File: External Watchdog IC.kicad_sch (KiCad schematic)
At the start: 5 parts, among them U4 TPS3823A-33DBVR

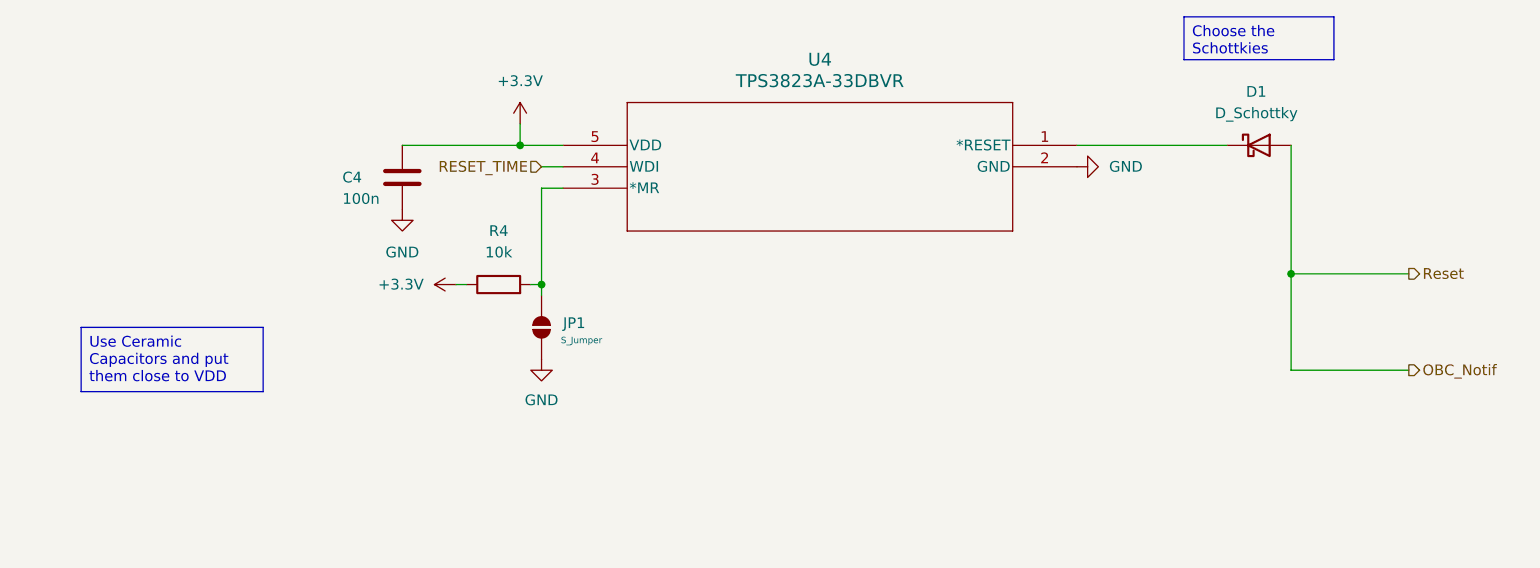
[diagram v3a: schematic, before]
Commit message: added current sensing and e-fuses
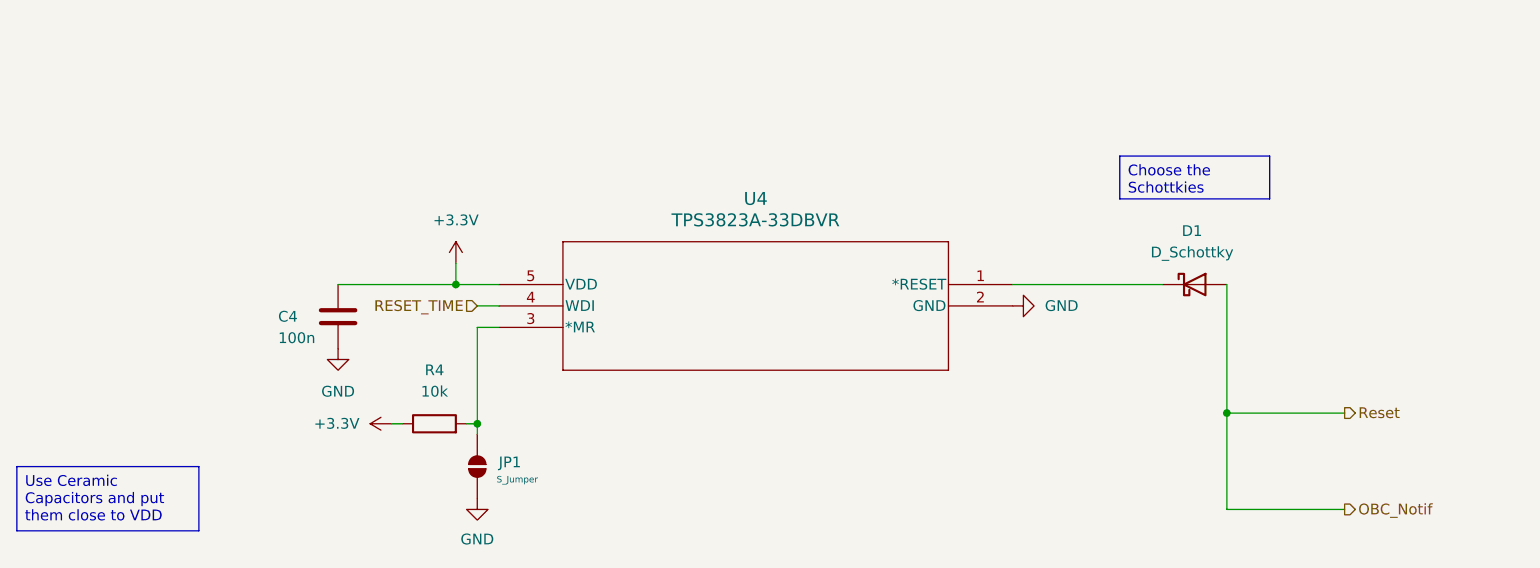
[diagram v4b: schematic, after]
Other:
- moved on the sheet: C4, D1, JP1, R4, U4

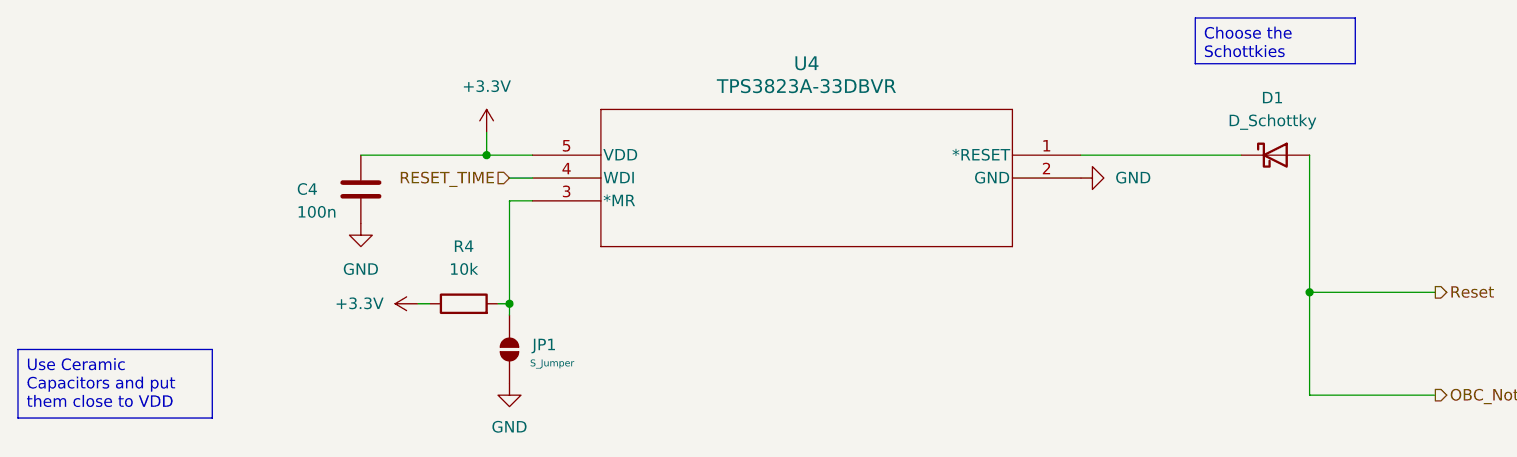
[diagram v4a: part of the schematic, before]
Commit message: Added connectors to schematic
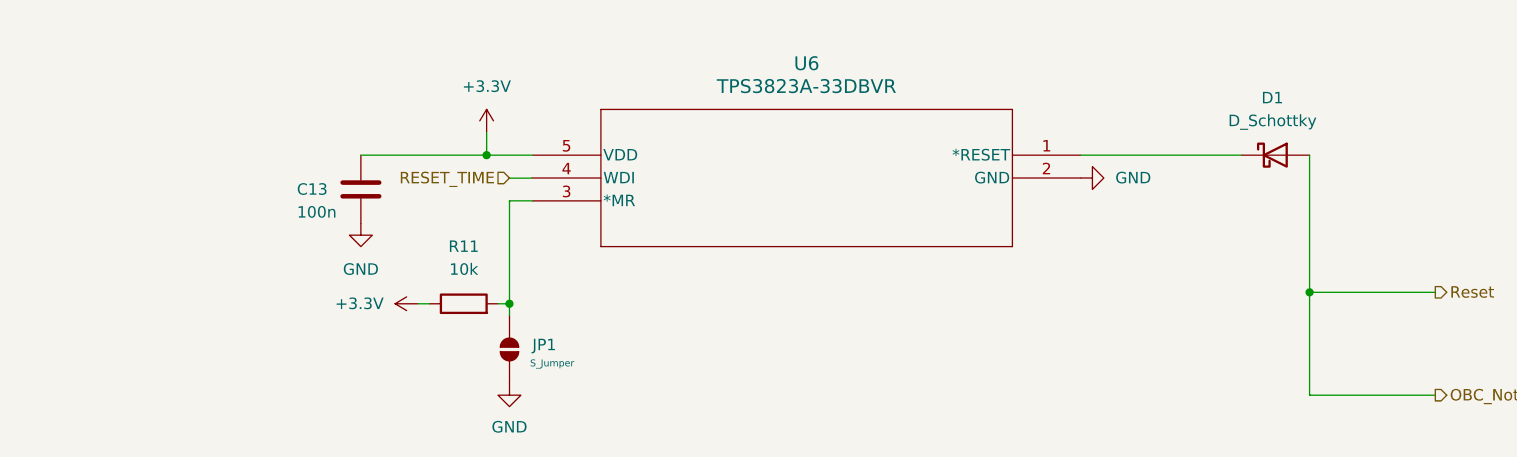
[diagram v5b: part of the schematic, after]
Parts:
- R11: renamed from R4; footprint (none) -> Resistor_SMD:R_0805_2012Metric; MANUFACTURER (none) -> Digikey; MANUFACTURER_PART_NUMBER (none) -> TNPW080510K0FEEA
- U6: renamed from U4; footprint DBV5 -> Package_TO_SOT_SMD:SOT-23-5_HandSoldering
- renumbered C4 to C13
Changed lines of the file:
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@@
 		(company "QSET (Jaron Cyna)")
-	)
-	(text_box "Use Ceramic Capacitors and put them close to VDD"
-		(exclude_from_sim no)
-		(at 55.88 110.49 0)
-		(size 21.59 7.62)
-		(margins 0.9525 0.9525 0.9525 0.9525)
-		(stroke
-			(width 0)
-			(type solid)
-		)
-		(fill
-			(type color)
-			(color 158 218 255 1)
-		)
-		(effects
-			(font
-				(size 1.27 1.27)
-			)
-			(justify left top)
-		)
-	)
-	(text_box "Choose the Schottkies"
-		(exclude_from_sim no)
-		(at 186.69 73.66 0)
-		(size 17.78 5.08)
-		(margins 0.9525 0.9525 0.9525 0.9525)
-		(stroke
-			(width 0)
-			(type solid)
-		)
-		(fill
-			(type color)
-			(color 158 218 255 1)
-		)
-		(effects
-			(font
-				(size 1.27 1.27)
-			)
-			(justify left top)
-		)
 	)
 	(junction
@@
 		(exclude_from_sim no)
 		(in_bom yes)
-		(on_board yes)
+		(on_board no)
 		(dnp no)
 		(fields_autoplaced yes)
@@
 		(dnp no)
 		(fields_autoplaced yes)
-		(property "Reference" "#PWR010"
+		(property "Reference" "#PWR026"
 			(at 93.98 102.87 0)
 			(effects
@@
 			(project ""
 				(path "/8f246f89-1ec7-4136-9977-839b50e116ed/61eb8b07-a516-4600-8bd8-c85438ae98cc"
-					(reference "#PWR010")
+					(reference "#PWR026")
 					(unit 1)
 				)
@@
 		(dnp no)
 		(fields_autoplaced yes)
-		(property "Reference" "R4"
+		(property "Reference" "R11"
 			(at 105.41 99.06 90)
 			(effects
@@
 			)
 		)
-		(property "Footprint" ""
+		(property "Footprint" "Resistor_SMD:R_0805_2012Metric"
 			(at 105.41 107.188 90)
 			(effects
@@
 			)
 		)
+		(property "MANUFACTURER_PART_NUMBER" "TNPW080510K0FEEA"
+			(at 105.41 105.41 0)
+			(effects
+				(font
+					(size 1.27 1.27)
+				)
+				(hide yes)
+			)
+		)
+		(property "MANUFACTURER" "Digikey"
+			(at 105.41 105.41 0)
+			(effects
+				(font
+					(size 1.27 1.27)
+				)
+				(hide yes)
+			)
+		)
 		(pin "1"
 		)
@@
 			(project "EPS_mppt_board"
 				(path "/8f246f89-1ec7-4136-9977-839b50e116ed/61eb8b07-a516-4600-8bd8-c85438ae98cc"
-					(reference "R4")
+					(reference "R11")
 					(unit 1)
 				)
@@
 		(on_board yes)
 		(dnp no)
-		(property "Reference" "C4"
+		(property "Reference" "C13"
 			(at 86.868 92.71 0)
 			(effects
@@
 			(project ""
 				(path "/8f246f89-1ec7-4136-9977-839b50e116ed/61eb8b07-a516-4600-8bd8-c85438ae98cc"
-					(reference "C4")
+					(reference "C13")
 					(unit 1)
 				)
@@
 		(dnp no)
 		(fields_autoplaced yes)
-		(property "Reference" "#PWR08"
+		(property "Reference" "#PWR024"
 			(at 107.95 90.17 0)
 			(effects
@@
 			(project ""
 				(path "/8f246f89-1ec7-4136-9977-839b50e116ed/61eb8b07-a516-4600-8bd8-c85438ae98cc"
-					(reference "#PWR08")
+					(reference "#PWR024")
 					(unit 1)
 				)
@@
 		(dnp no)
 		(fields_autoplaced yes)
-		(property "Reference" "#PWR011"
+		(property "Reference" "#PWR027"
 			(at 104.14 105.41 0)
 			(effects
@@
 			(project "EPS_mppt_board"
 				(path "/8f246f89-1ec7-4136-9977-839b50e116ed/61eb8b07-a516-4600-8bd8-c85438ae98cc"
-					(reference "#PWR011")
+					(reference "#PWR027")
 					(unit 1)
 				)
@@
 		(on_board yes)
 		(dnp no)
-		(property "Reference" "U4"
+		(property "Reference" "U6"
 			(at 143.51 78.74 0)
 			(effects
@@
 			)
 		)
-		(property "Footprint" "DBV5"
+		(property "Footprint" "Package_TO_SOT_SMD:SOT-23-5_HandSoldering"
 			(at 173.99 88.9 0)
 			(effects
@@
 			(project ""
 				(path "/8f246f89-1ec7-4136-9977-839b50e116ed/61eb8b07-a516-4600-8bd8-c85438ae98cc"
-					(reference "U4")
+					(reference "U6")
 					(unit 1)
 				)
@@
 			)
 		)
-		(property "Datasheet" "~"
+		(property "Datasheet" ""
 			(at 110.49 110.49 0)
 			(effects
@@
 		(dnp no)
 		(fields_autoplaced yes)
-		(property "Reference" "#PWR09"
+		(property "Reference" "#PWR025"
 			(at 180.34 91.44 0)
 			(effects
@@
 			(project "EPS_mppt_board"
 				(path "/8f246f89-1ec7-4136-9977-839b50e116ed/61eb8b07-a516-4600-8bd8-c85438ae98cc"
-					(reference "#PWR09")
+					(reference "#PWR025")
 					(unit 1)
 				)
@@
 		(on_board yes)
 		(dnp no)
-		(property "Reference" "#PWR012"
+		(property "Reference" "#PWR028"
 			(at 110.49 120.65 0)
 			(effects
@@
 			(project "EPS_mppt_board"
 				(path "/8f246f89-1ec7-4136-9977-839b50e116ed/61eb8b07-a516-4600-8bd8-c85438ae98cc"
-					(reference "#PWR012")
-					(unit 1)
-				)
+					(reference "#PWR028")
+					(unit 1)
+				)

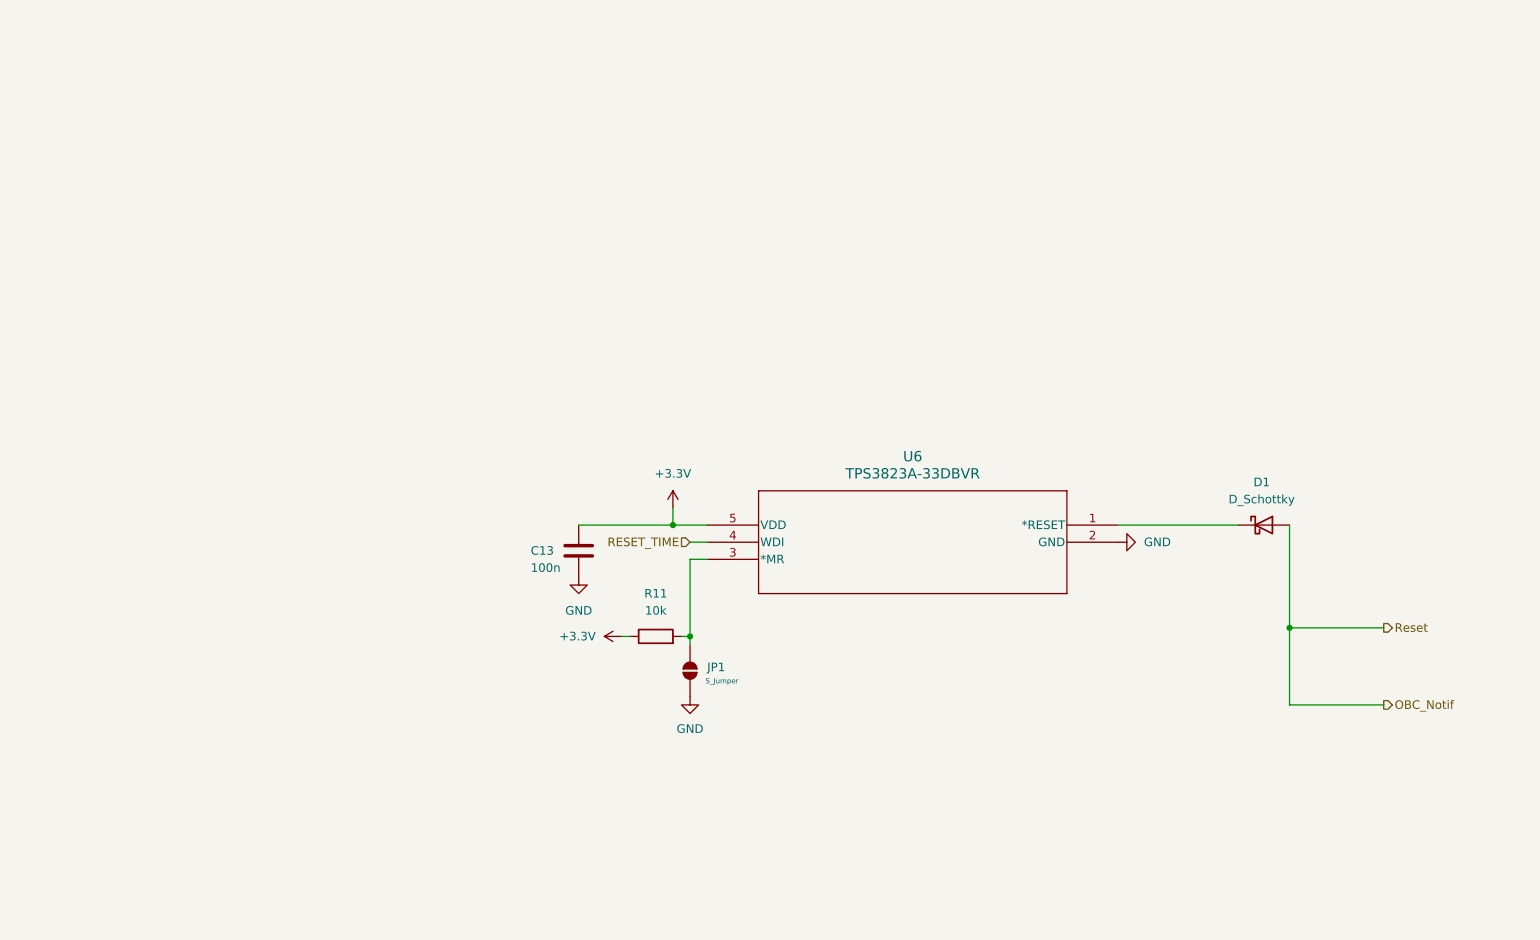
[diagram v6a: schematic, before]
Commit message: Small schematic changes
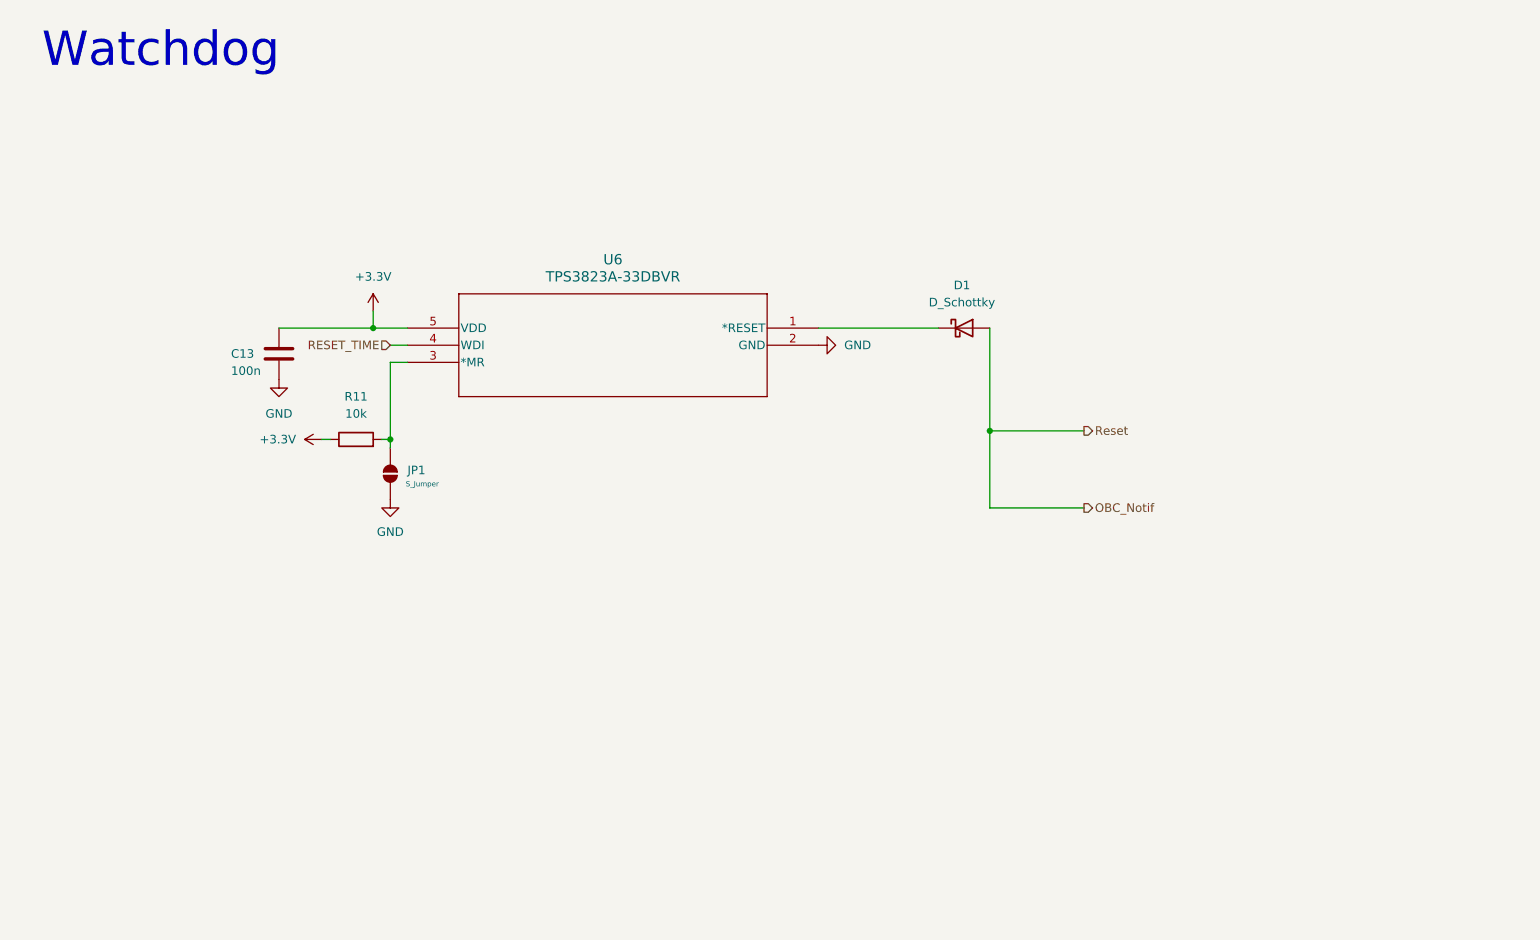
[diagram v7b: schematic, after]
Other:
- note added: "Watchdog"
- moved on the sheet: C13, D1, JP1, R11, U6

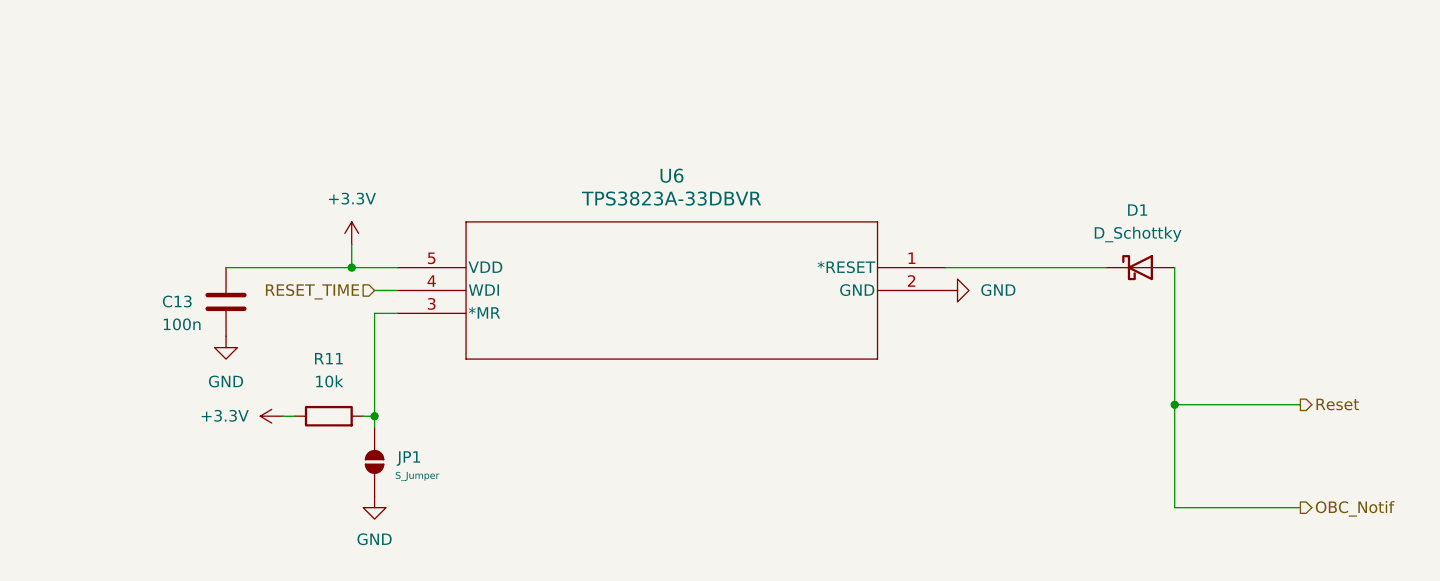
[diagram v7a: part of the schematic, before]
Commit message: Changed LTC 4412 to 4417, still kinks to work out
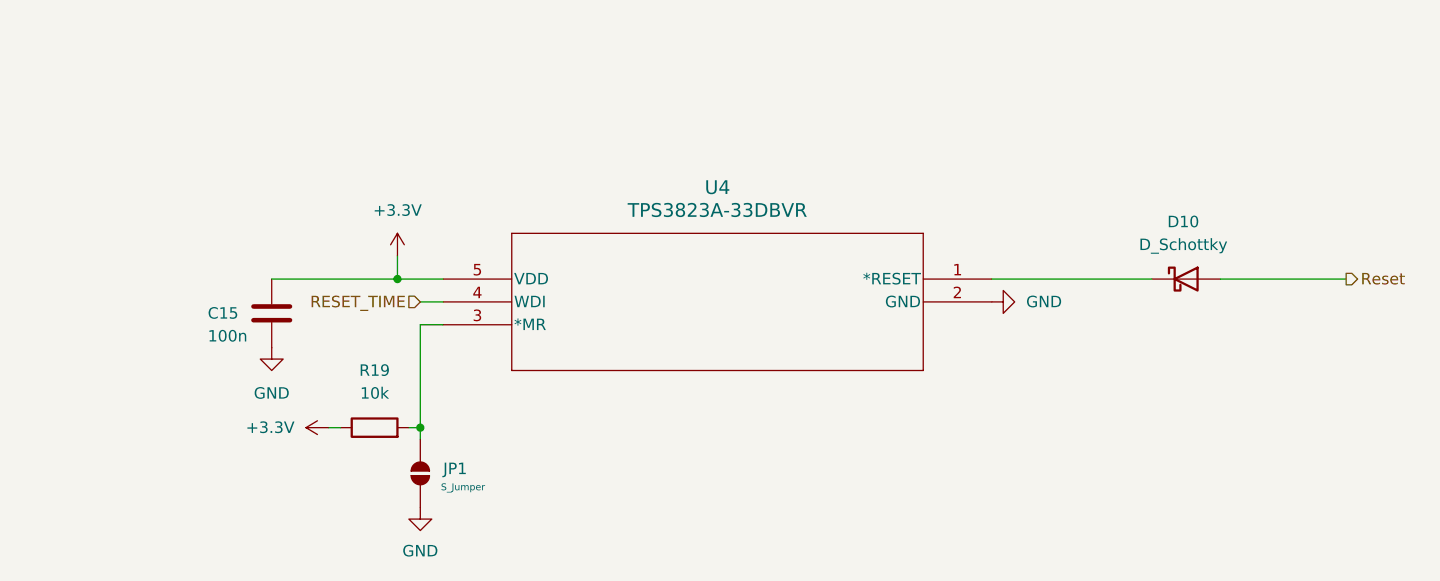
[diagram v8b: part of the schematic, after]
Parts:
- removed D1: D_Schottky, Diode_SMD:D_SOD-323F, symbol Device:D_Schottky
- added D10: D_Schottky, Diode_SMD:D_0603_1608Metric, symbol Device:D_Schottky
- renumbered C13 to C15, R11 to R19, U6 to U4
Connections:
- net at U4.1 (*RESET): now also D10.1 (K)
- new net Reset: D10.2 (A)
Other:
- moved on the sheet: C15, JP1, R19, U4
